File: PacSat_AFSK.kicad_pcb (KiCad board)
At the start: 6 copper layers, 92 x 92 mm, 308 parts, among them J10 2118718-2, J11 Molex 73251-1153, J2 FTSH-105-01-L-DV-K, J3 2118714-2, J4 2118714-2, J5 2118714-2, J6 2118714-2, J7 2118714-2, J8 Molex 73251-1153, J9 2118714-2, P10 CONUFL001-SMD-T, P11 CONUFL001-SMD-T, P12 CONUFL001-SMD-T, P13 CONUFL001-SMD-T, P14 Conn_04x26_Pin, P2 CONUFL001-SMD-T, P3 CONUFL001-SMD-T, P4 CONUFL001-SMD-T, P5 CONUFL001-SMD-T, P6 CONUFL001-SMD-T, P7 CONUFL001-SMD-T, P9 CONUFL001-SMD-T, Q2 BSS138, Q3 DMP2037U, Q4 DMP2037U, Q5 DMP2037U, Q6 DMP2037U, Q7 DMP2037U, U10 MAX4495AAUT, U11 MAX4495AAUT, U12 MAX31331TETB+, U13 AS1016204-0108X0PWAY, U14 TCAN1044ADDFRQ1, U15 AX5043, U17 AX5043, U19 AX5043, U2 TMS570LS0914PGE, U21 AX5043, U23 AX5043, U25 QPL9547, U26 RBP-140+, U27 TQP7M9106, U28 ADL5501AKSZ-R2, U29 ADL5501AKSZ-R2, U3 CDCLVC1106, U4 TPSM828302ARDSR, U5 LP3962EMP-3.3/NOPB, U6 STWD100NYWY3F, U8 MP5073GG-P, U9 MAX4495AAUT, Y2 O 16,0-JT22CT-A-P-3,3-LF, Y3 32.768kHz

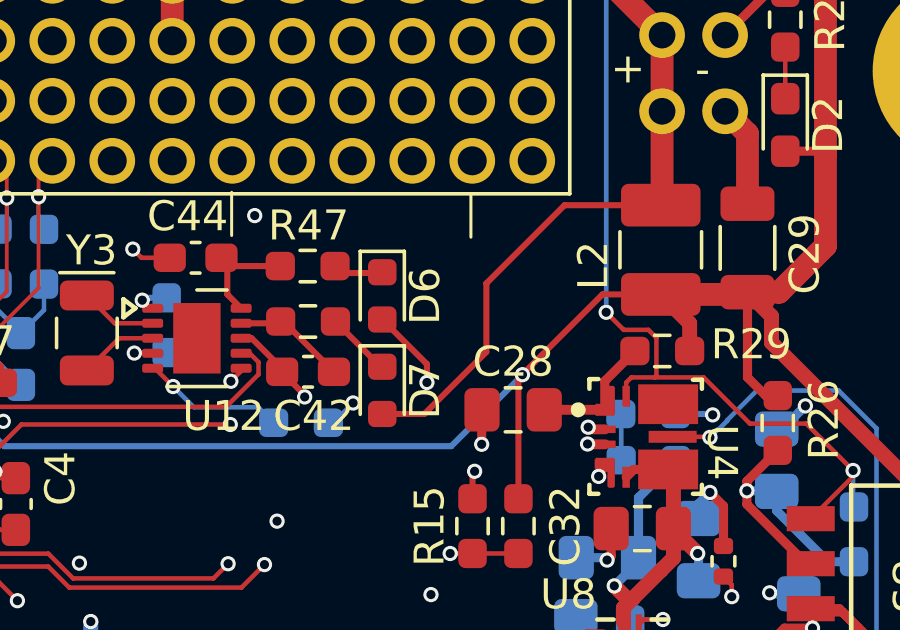
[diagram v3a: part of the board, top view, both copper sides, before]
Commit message: Add some notes, fix the diode footprints on the RTC
Signed-off-by: Corey Minyard <corey@minyard.net>
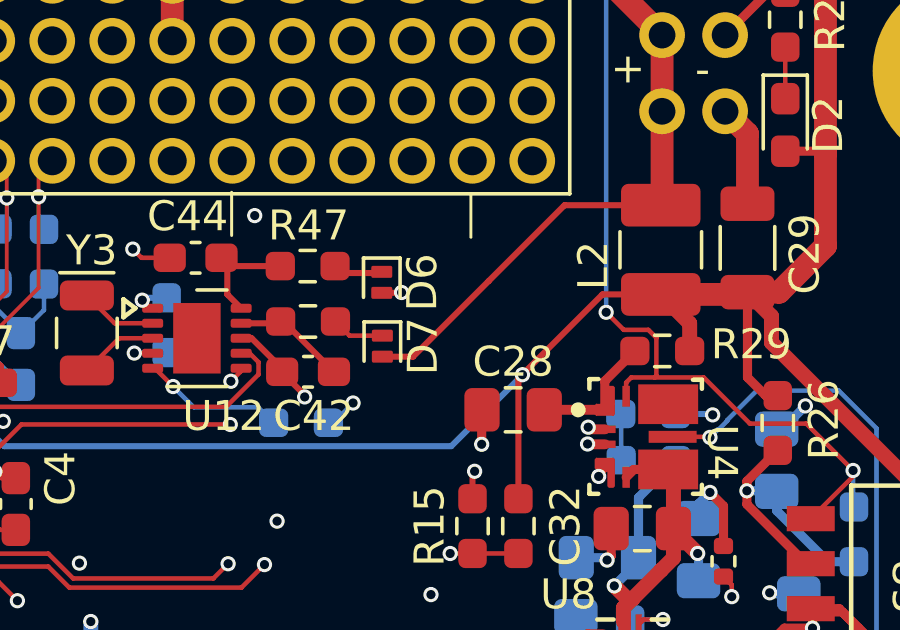
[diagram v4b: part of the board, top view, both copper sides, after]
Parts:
- D6, D7: footprint Diode_SMD:D_0603_1608Metric -> Diode_SMD:D_SOD-882
- moved D7 1.47 mm to (216.0, 73.7)
- moved D6 0.45 mm to (216.0, 71.5)
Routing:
- net VSYS: track 39.5 -> 37.4 mm
- net +3.3V: track 160.5 -> 158.4 mm
